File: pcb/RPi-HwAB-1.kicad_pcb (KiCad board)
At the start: 6 copper layers, 65 x 56 mm, 160 parts, among them J1 GPIO, J2 Hirose_FH12-16S, J3 TC2030, U1 CAT24C256, U10 MX25L12835F, U11 INA230AIRGTT, U12 INA230AIRGTT, U13 INA230AIRGTT, U14 MCP9804_DFN, U2 TPSM82903, U3 TLV74312PDBVR, U4 TPSM82903, U5 AP3441SHE-7B, U6 AP3441SHE-7B, U7 XC7A100T-FGG484, U9 MT41K256M16LY, Y1 SiT9365AI-2B2-33E200.000000

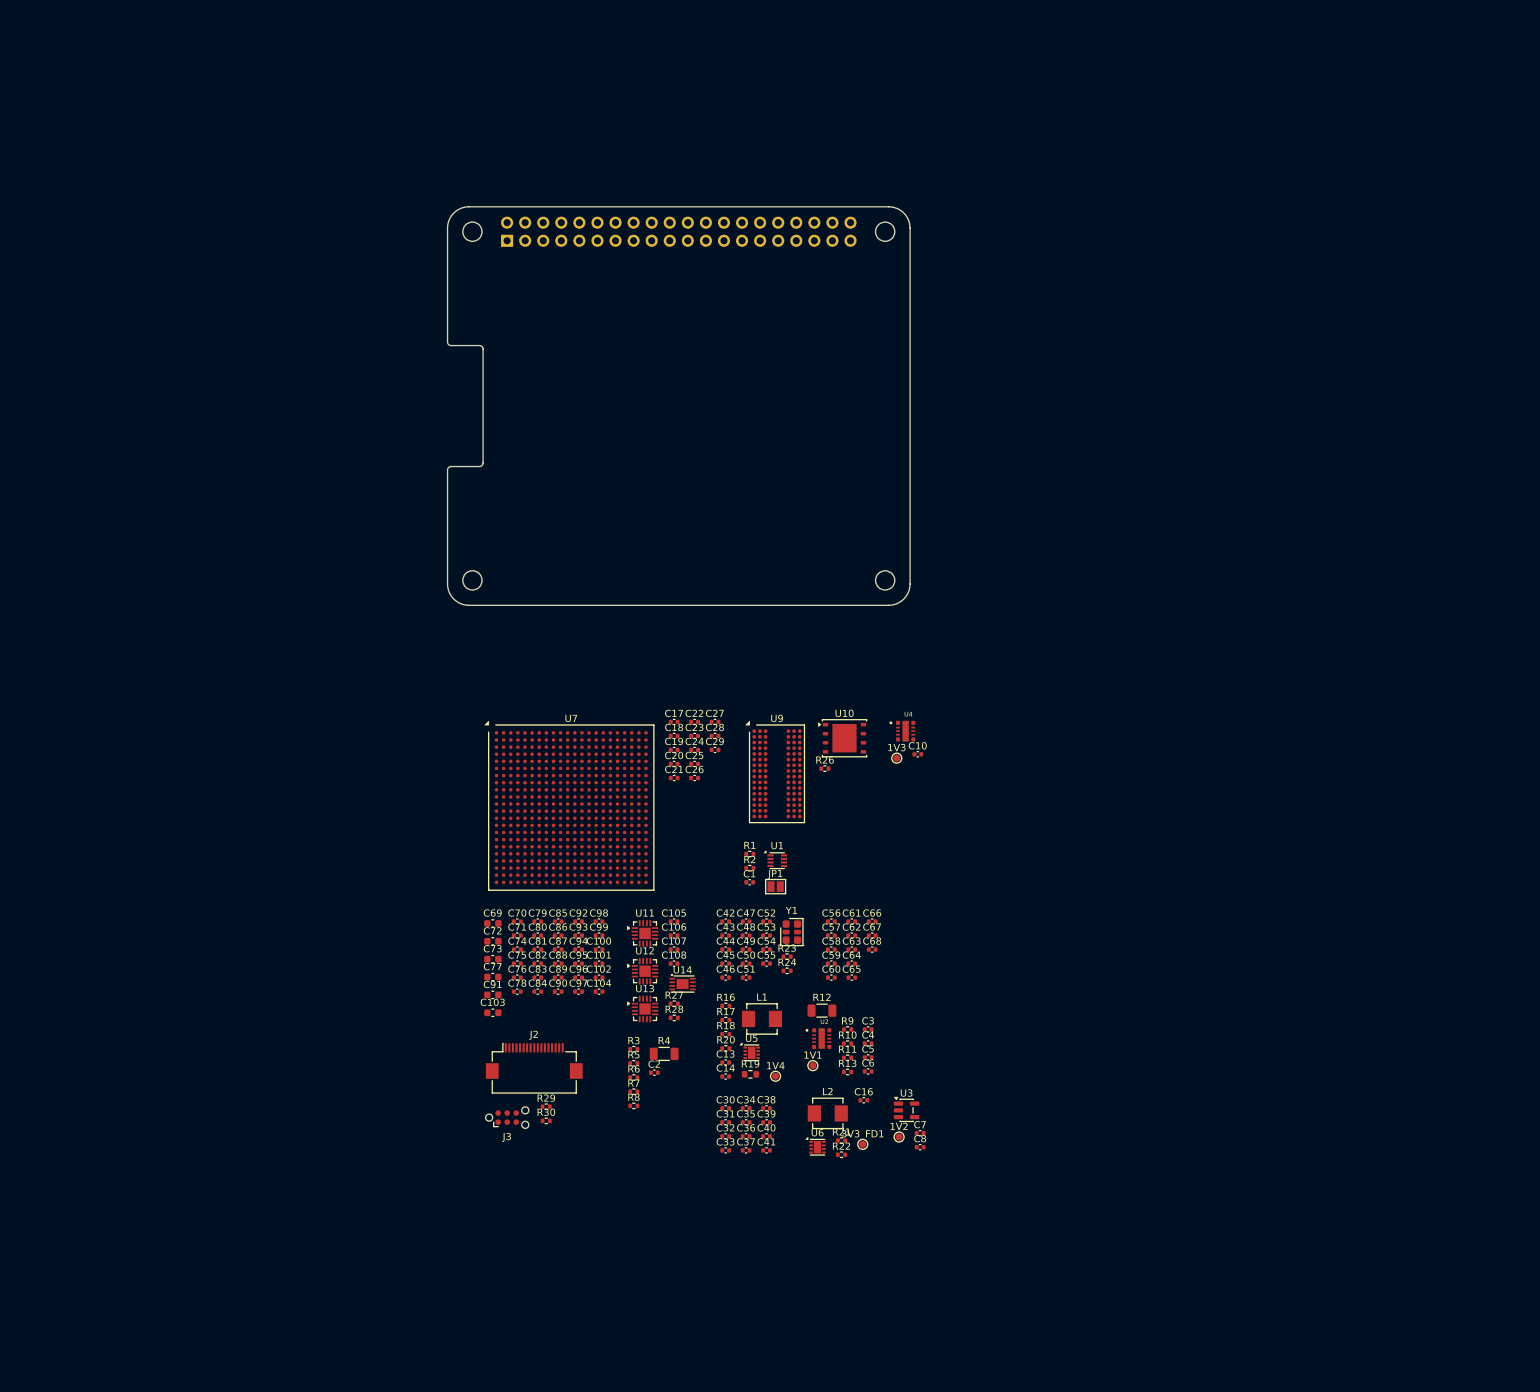
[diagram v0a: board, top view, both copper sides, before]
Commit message: initial layout, dogbone fanout
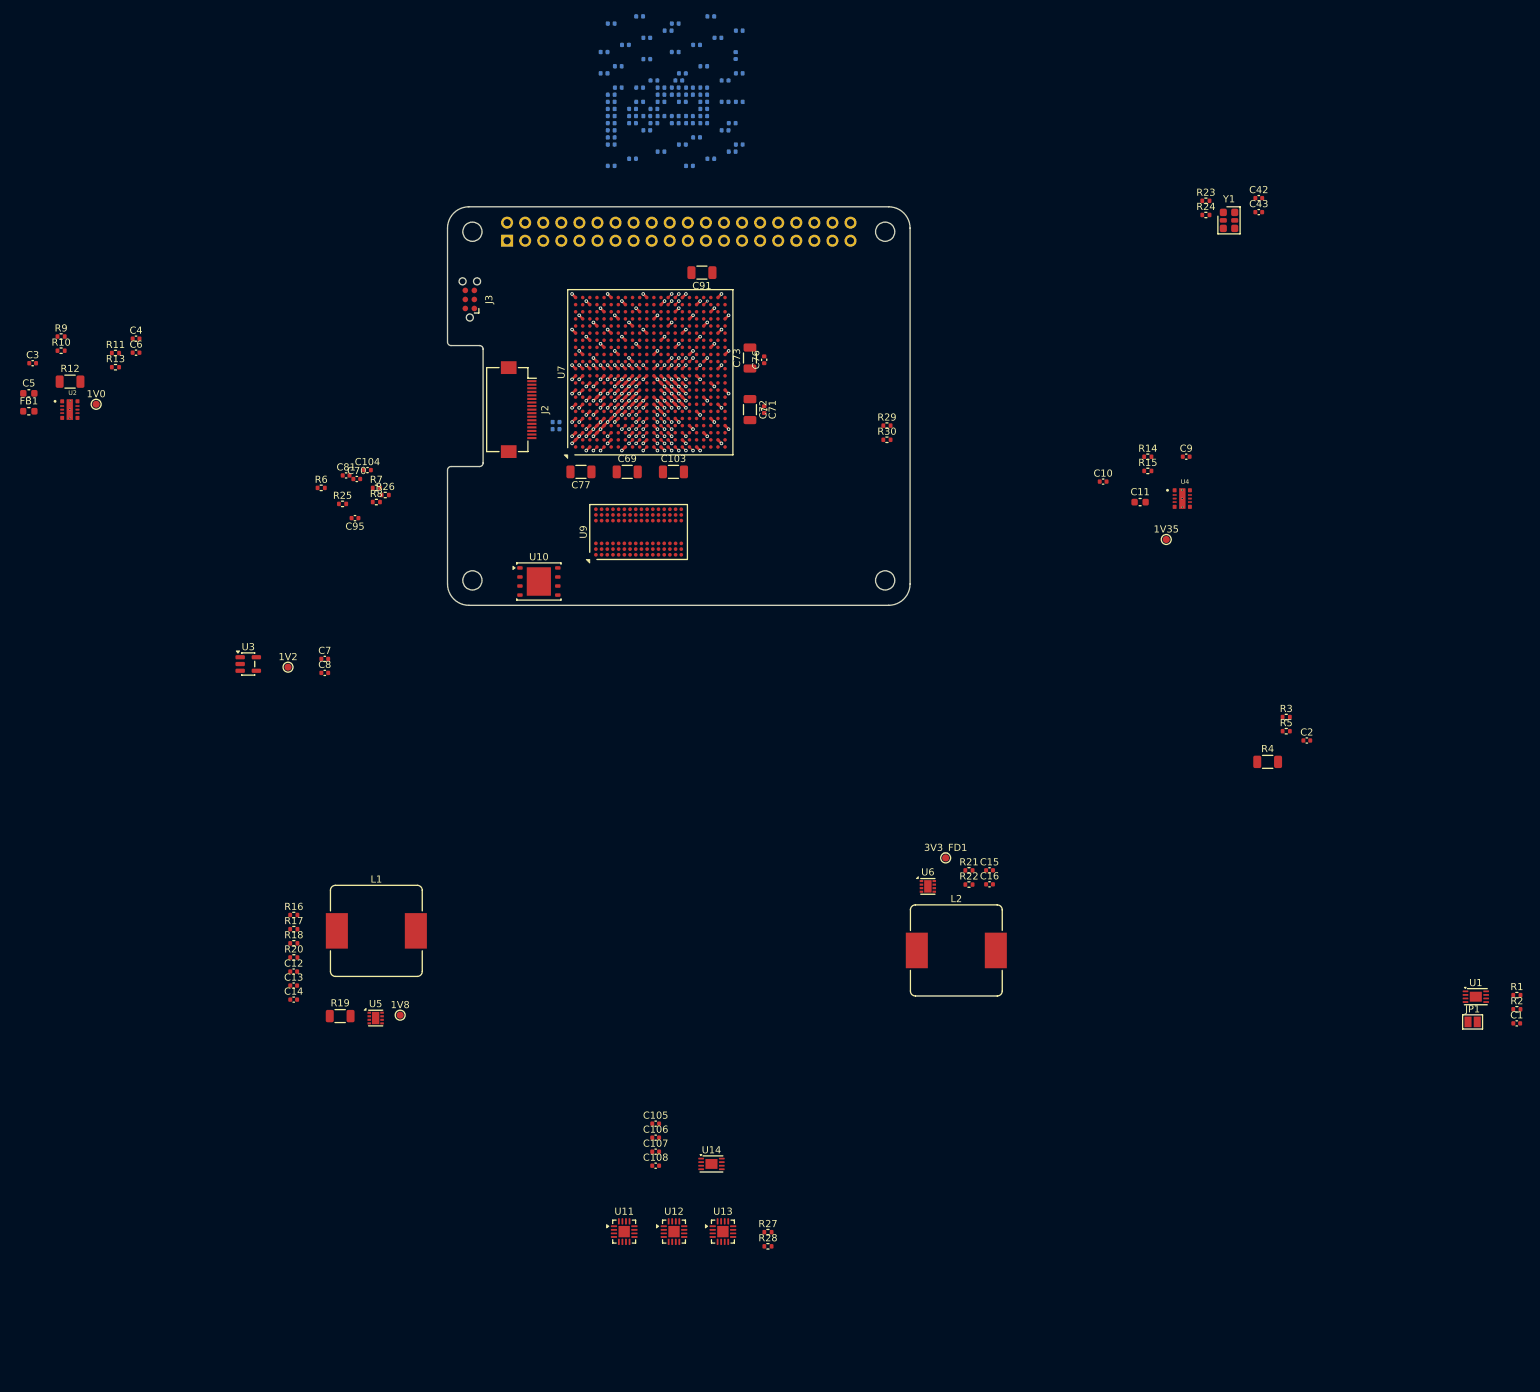
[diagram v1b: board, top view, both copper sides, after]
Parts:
- removed 1V1, 1V3, 1V4: TestPoint, TestPoint:TestPoint_Pad_D1.0mm
- added 1V0: TestPoint, TestPoint:TestPoint_Pad_D1.0mm, F.Cu at (50.6, 71.8)
- added 1V35: TestPoint, TestPoint:TestPoint_Pad_D1.0mm, F.Cu at (201.0, 90.8)
- added 1V8: TestPoint, TestPoint:TestPoint_Pad_D1.0mm, F.Cu at (93.3, 157.6)
- added C11: 22uF, Capacitor_SMD:C_0603_1608Metric, F.Cu at (197.3, 85.5)
- added C12: 10uF, Capacitor_SMD:C_0402_1005Metric, F.Cu at (78.4, 151.5)
- added C15: 10uF, Capacitor_SMD:C_0402_1005Metric, F.Cu at (176.2, 137.2)
- added C9: 10uF, Capacitor_SMD:C_0402_1005Metric, F.Cu at (203.8, 79.1)
- added FB1: 120R @ 100MHz, Inductor_SMD:L_0603_1608Metric, F.Cu at (41.2, 72.7)
- added R14: 15K 1%, Resistor_SMD:R_0402_1005Metric, F.Cu at (198.4, 79.1)
- added R15: 12K 1%, Resistor_SMD:R_0402_1005Metric, F.Cu at (198.4, 81.1)
- added R25: 1K, Resistor_SMD:R_0402_1005Metric, F.Cu at (85.2, 85.8)
- C1: value 100n -> 0.1uF
- C100, C101, C102, C17, C18, C19, C20, C21, C22, C23, C24, C25, C26, C27, C28, C29, C30, C31, C32, C33, C34, C35, C36, C37, C38, C39, C40, C41, C44, C45, C46, C47, C48, C49, C50, C51, C52, C53, C54, C55, C56, C57, C58, C59, C60, C61, C62, C63, C64, C65, C66, C67, C68, C74, C75, C78, C79, C80, C82, C83, C84, C85, C86, C87, C88, C89, C90, C92, C93, C94, C96, C97, C98, C99: moved to B.Cu
- C103, C69, C72, C73, C77, C91: footprint Capacitor_SMD:C_0603_1608Metric -> Capacitor_SMD:C_1206_3216Metric
- C3: footprint library:C_0402_1005Metric -> Capacitor_SMD:C_0402_1005Metric
- C5: footprint library:C_0402_1005Metric -> Capacitor_SMD:C_0603_1608Metric
- L1, L2: footprint Inductor_SMD:L_Vishay_IHLP-1616 -> Inductor_SMD:L_Bourns_SRP1245A
- R10, R29, R6, R7, R8, R9: footprint library:R_0402_1005Metric -> Resistor_SMD:R_0402_1005Metric
- R19: footprint Resistor_SMD:R_0603_1608Metric -> Resistor_SMD:R_1206_3216Metric
- U1: footprint Package_DFN_QFN:DFN-8_2x2mm_P0.5mm -> Package_DFN_QFN:DFN-8-1EP_3x2mm_P0.5mm_EP1.7x1.4mm
- U11, U12, U13: value INA230AIRGTT -> INA230AIRGTR
- U14: value MCP9804_DFN -> MCP9804T-E/MC
- U9: value MT41K256M16LY -> MT41K256M16TW-107:P TR
- moved C37 159.5 mm to (123.0, 18.2)
- moved C41 155.7 mm to (135.0, 21.2), turned to 180 degrees
- moved C32 154.4 mm to (138.0, 20.2), turned to 180 degrees
- moved C36 150.5 mm to (136.0, 24.2), turned to 180 degrees
- moved C5 150.4 mm to (41.2, 70.2)
- moved C3 150.2 mm to (41.7, 66.0)
- moved C39 149.2 mm to (122.0, 25.2), turned to 180 degrees
- moved C30 147.9 mm to (128.0, 23.2), turned to 180 degrees
- moved C40 147.6 mm to (136.0, 27.2), turned to 180 degrees
- moved C33 147.4 mm to (139.0, 29.2)
- moved R9 147.3 mm to (45.7, 62.2)
- moved R10 147.3 mm to (45.7, 64.2)
- moved C35 146.4 mm to (139.0, 26.2), turned to 180 degrees
- moved C34 145.0 mm to (129.0, 26.2), turned to 180 degrees
- moved C38 144.5 mm to (127.0, 27.2), turned to 180 degrees
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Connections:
- C105 pad 1: /Connectors/3V3 -> /Sensors/3V3_RPi
- C106 pad 1: /Connectors/3V3 -> /Sensors/3V3_RPi
- C107 pad 1: /Connectors/3V3 -> /Sensors/3V3_RPi
- C108 pad 1: /Connectors/3V3 -> /Sensors/3V3_RPi
- J1 pad 1: /Connectors/3V3 -> /Connectors/3V3_RPi
- J1 pad 17: /Connectors/3V3 -> /Connectors/3V3_RPi
- R27 pad 1: /Connectors/3V3 -> /Sensors/3V3_RPi
- R28 pad 1: /Connectors/3V3 -> /Sensors/3V3_RPi
- R30 pad 1: /Connectors/3V3 -> /Connectors/3V3_RPi
- U11 pad 8: /Connectors/3V3 -> /Sensors/3V3_RPi
- U12 pad 2: /Connectors/3V3 -> /Sensors/3V3_RPi
- U12 pad 8: /Connectors/3V3 -> /Sensors/3V3_RPi
- U13 pad 2: /Connectors/3V3 -> /Sensors/3V3_RPi
- U13 pad 8: /Connectors/3V3 -> /Sensors/3V3_RPi
- U14 pad 8: /Connectors/3V3 -> /Sensors/3V3_RPi
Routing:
- net GND: track 0.00 -> 79.9 mm, vias 0 -> 90
- net /Main Power/1V0_FD: track 0.00 -> 18.4 mm, vias 0 -> 18
- net /Main Power/3V3_FD: track 0.00 -> 17.7 mm, vias 0 -> 25
- net /Main Power/1V35_DDR: track 0.00 -> 8.49 mm, vias 0 -> 12
- net /Main Power/1V8_FD: track 0.00 -> 4.24 mm, vias 0 -> 6
- net /Main Power/1V2_MGT: track 0.00 -> 4.24 mm, vias 0 -> 6
- net /Main Power/1V0_MGT: track 0.00 -> 3.54 mm, vias 0 -> 5
- net /FPGA/FPGA 3/WEn: track 0.00 -> 0.71 mm, vias 0 -> 1
- net /FPGA/FPGA 3/UDQS_P: track 0.00 -> 0.71 mm, vias 0 -> 1
- net /FPGA/FPGA 3/UDQS_N: track 0.00 -> 0.71 mm, vias 0 -> 1
- net /FPGA/FPGA 3/UDM: track 0.00 -> 0.71 mm, vias 0 -> 1
- net /FPGA/FPGA 3/RESETn: track 0.00 -> 0.71 mm, vias 0 -> 1
- net /FPGA/FPGA 3/RASn: track 0.00 -> 0.71 mm, vias 0 -> 1
- net /FPGA/FPGA 3/ODT: track 0.00 -> 0.71 mm, vias 0 -> 1
- net /FPGA/FPGA 3/LDQS_P: track 0.00 -> 0.71 mm, vias 0 -> 1
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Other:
- copper layers 6 -> 4
- board text removed: "DISPLAY (OPTIONAL)"
- board text removed: "Extend PCB edge 0.5mm if using SMT header"
- board text removed: "PoE"
- board text removed: "RJ45"
- board text removed: "USB"

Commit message: added mig ddr pinout constraints
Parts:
- removed C100, C101, C102, C105, C106, C107, C108, C74, C75, C78, C79, C80, C82, C83, C84, C85, C86, C87, C88, C89, C90, C92, C93, C94, C96, C97, C98, C99: 0.1uF, Capacitor_SMD:C_0402_1005Metric
- removed C103, C72, C73, C77, C91: 47uF, Capacitor_SMD:C_1206_3216Metric
- removed C104, C71, C76, C81, C95: 10uF, Capacitor_SMD:C_0402_1005Metric
- C10, C16: value 4.7nF -> 10uF; footprint Capacitor_SMD:C_0402_1005Metric -> Capacitor_SMD:C_1206_3216Metric
- C11: value 22uF -> 4.7nF; footprint Capacitor_SMD:C_0603_1608Metric -> Capacitor_SMD:C_0402_1005Metric
- C12, C15: value 10uF -> 4.7nF
- C13, C4: value 4.7nF -> 0.1uF
- C14: value 0.1uF -> 10uF; footprint Capacitor_SMD:C_0402_1005Metric -> Capacitor_SMD:C_1206_3216Metric
- C3, C9: value 10uF -> 22uF; footprint Capacitor_SMD:C_0402_1005Metric -> Capacitor_SMD:C_0603_1608Metric
- C37, C38, C67, C68: moved to F.Cu
- C42, C43: moved to B.Cu
- C44, C46, C48, C50, C52, C62: value 0.1uF -> 10uF; footprint Capacitor_SMD:C_0402_1005Metric -> Capacitor_SMD:C_1206_3216Metric; moved to F.Cu
- C45, C47, C49, C51, C57, C63: value 0.1uF -> 4.7uF; footprint Capacitor_SMD:C_0402_1005Metric -> Capacitor_SMD:C_0603_1608Metric; moved to F.Cu
- C5: value 22uF -> 10uF; footprint Capacitor_SMD:C_0603_1608Metric -> Capacitor_SMD:C_1206_3216Metric
- C6: value 0.1uF -> 4.7nF
- C69: value 47uF -> 0.1uF; footprint Capacitor_SMD:C_1206_3216Metric -> Capacitor_SMD:C_0402_1005Metric
- C70: value 10uF -> 0.1uF
- R10: value 15K 1% -> 10K 1%
- R12, R19: value 0.005 -> 10; footprint Resistor_SMD:R_1206_3216Metric -> Resistor_SMD:R_0402_1005Metric
- R13, R20: value 10 -> 15K 1%
- R16: value 30K 1% -> 0.005; footprint Resistor_SMD:R_0402_1005Metric -> Resistor_SMD:R_1206_3216Metric
- R17: value 15K 1% -> 30K 1%
- R29: value 100K -> 2.2K
- R3: value 10 -> 0.003 1%; footprint Resistor_SMD:R_0402_1005Metric -> Resistor_SMD:R_1206_3216Metric
- R30: value 2.2K -> 100K
- R4: value 0.003 1% -> 10; footprint Resistor_SMD:R_1206_3216Metric -> Resistor_SMD:R_0402_1005Metric
- R9: value 10K 1% -> 0.005; footprint Resistor_SMD:R_0402_1005Metric -> Resistor_SMD:R_1206_3216Metric
- U10: value MX25L12835F -> MT41K256M16TW-107:P TR; footprint Package_SON:WSON-8-1EP_6x5mm_P1.27mm_EP3.4x4mm -> Package_BGA:Micron_FBGA-96_7.5x13.5mm_Layout9x16_P0.8mm
- U12: value INA230AIRGTR -> MCP9804T-E/MC; footprint Package_DFN_QFN:VQFN-16-1EP_3x3mm_P0.5mm_EP1.6x1.6mm -> Package_DFN_QFN:DFN-8-1EP_3x2mm_P0.5mm_EP1.7x1.4mm
- U14: value MCP9804T-E/MC -> INA230AIRGTR; footprint Package_DFN_QFN:DFN-8-1EP_3x2mm_P0.5mm_EP1.7x1.4mm -> Package_DFN_QFN:VQFN-16-1EP_3x3mm_P0.5mm_EP1.6x1.6mm
- U9: value MT41K256M16TW-107:P TR -> MX25L12835F; footprint Package_BGA:Micron_FBGA-96_7.5x13.5mm_Layout9x16_P0.8mm -> Package_SON:WSON-8-1EP_6x5mm_P1.27mm_EP3.4x4mm
- moved C55 176.0 mm to (92.8, 208.2)
- moved C56 176.0 mm to (85.8, 201.2)
- moved C58 168.6 mm to (93.2, 199.2)
- moved C59 168.6 mm to (93.2, 198.2)
- moved C60 168.6 mm to (96.2, 197.2)
- moved C61 168.6 mm to (93.2, 197.2)
- moved C64 168.6 mm to (96.2, 198.2)
- moved C65 168.6 mm to (93.2, 194.2)
- moved C66 168.6 mm to (93.2, 196.2)
- moved C53 161.0 mm to (89.8, 188.8)
- moved C54 161.0 mm to (94.8, 186.8)
- moved C42 88.7 mm to (131.5, 75.2)
- moved C43 86.7 mm to (131.5, 71.2)
- moved C30 72.9 mm to (159.5, 89.0)
- moved C29 67.7 mm to (159.5, 87.5)
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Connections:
- net +3V3 renamed 3V3_RPi
- C10 pad 1: Net-(U4-SS/TR) -> /Main Power/5V0_N
- C11 pad 1: /Main Power/1V35_DDR -> Net-(U4-SS/TR)
- C12 pad 1: /Main Power/5V0_N -> /Main Power/1V8/1V8_P
- C12 pad 2: GND -> /Main Power/1V8/1V8_FB
- C13 pad 1: /Main Power/1V8/1V8_P -> /Main Power/1V8_SENS_N
- C13 pad 2: /Main Power/1V8/1V8_FB -> /Main Power/1V8_SENS_P
- C14 pad 1: /Main Power/1V8_SENS_N -> /Main Power/5V0_N
- C14 pad 2: /Main Power/1V8_SENS_P -> GND
- C15 pad 1: /Main Power/5V0_N -> /Main Power/3V3_FD
- C15 pad 2: GND -> /Main Power/3V3/3V3_FB
- C16 pad 1: /Main Power/3V3_FD -> /Main Power/5V0_N
- C16 pad 2: /Main Power/3V3/3V3_FB -> GND
- C29 pad 1: GND -> Net-(U7E-IO_L12N_T1_MRCC_34)
- C29 pad 2: /Main Power/3V3_FD -> Net-(Y1-OUT-)
- C3 pad 1: /Main Power/5V0_N -> /Main Power/1V0/1V0_P
- C30 pad 1: GND -> Net-(U7E-IO_L12P_T1_MRCC_34)
- C30 pad 2: /Main Power/3V3_FD -> Net-(Y1-OUT+)
- C31 pad 2: /Main Power/3V3_FD -> /Main Power/1V35_DDR
- C32 pad 2: /Main Power/3V3_FD -> /Main Power/1V35_DDR
- C33 pad 2: /Main Power/3V3_FD -> /Main Power/1V35_DDR
- C34 pad 2: /Main Power/3V3_FD -> /Main Power/1V35_DDR
- C35 pad 2: /Main Power/3V3_FD -> /Main Power/1V35_DDR
- C36 pad 2: /Main Power/3V3_FD -> /Main Power/1V35_DDR
- C37 pad 1: GND -> /FPGA/FPGA 4/F2P_P
- C37 pad 2: /Main Power/3V3_FD -> /Connectors/PCIE.F2P_N
- C38 pad 1: GND -> /FPGA/FPGA 4/F2P_N
- C38 pad 2: /Main Power/3V3_FD -> /Connectors/PCIE.F2P_P
- C39 pad 2: /Main Power/3V3_FD -> /Main Power/1V0_MGT
- C4 pad 1: Net-(U2-SS/TR) -> /Main Power/1V0_SENS_N
- C4 pad 2: GND -> /Main Power/1V0_SENS_P
- C40 pad 2: /Main Power/3V3_FD -> /Main Power/1V0_MGT
- C41 pad 2: /Main Power/3V3_FD -> /Main Power/1V2_MGT
- C42 pad 1: Net-(U7E-IO_L12N_T1_MRCC_34) -> GND
- C42 pad 2: Net-(Y1-OUT-) -> /Main Power/1V2_MGT
- C43 pad 1: Net-(U7E-IO_L12P_T1_MRCC_34) -> GND
- C43 pad 2: Net-(Y1-OUT+) -> /Main Power/1V2_MGT
- C44 pad 1: GND -> /Main Power/1V0_MGT
- C44 pad 2: /Main Power/1V35_DDR -> GND
- C45 pad 1: GND -> /Main Power/1V0_MGT
- C45 pad 2: /Main Power/1V35_DDR -> GND
- C46 pad 1: GND -> /Main Power/1V2_MGT
- C46 pad 2: /Main Power/1V35_DDR -> GND
- C47 pad 1: GND -> /Main Power/1V2_MGT
- C47 pad 2: /Main Power/1V35_DDR -> GND
- C48 pad 1: GND -> /Main Power/3V3_FD
- C48 pad 2: /Main Power/1V35_DDR -> GND
- C49 pad 1: GND -> /Main Power/3V3_FD
- C49 pad 2: /Main Power/1V35_DDR -> GND
- C5 pad 1: /Main Power/1V0/1V0_P -> /Main Power/5V0_N
- C50 pad 1: GND -> /Main Power/1V35_DDR
- C50 pad 2: /Main Power/1V35_DDR -> GND
- C51 pad 1: GND -> /Main Power/1V35_DDR
- C51 pad 2: /Main Power/1V35_DDR -> GND
- C52 pad 1: GND -> /Main Power/1V0_FD
- C52 pad 2: /Main Power/1V35_DDR -> GND
- C53 pad 2: /Main Power/1V35_DDR -> /Main Power/1V0_FD
- C54 pad 2: /Main Power/1V35_DDR -> /Main Power/1V0_FD
- C55 pad 2: /Main Power/1V35_DDR -> /Main Power/1V0_FD
- C56 pad 2: /Main Power/1V0_MGT -> /Main Power/1V0_FD
- C57 pad 1: GND -> /Main Power/1V0_FD
- C57 pad 2: /Main Power/1V2_MGT -> GND
- C58 pad 2: /Main Power/1V0_MGT -> /Main Power/1V0_FD
- C59 pad 2: /Main Power/1V2_MGT -> /Main Power/1V0_FD
- C6 pad 1: /Main Power/1V0_SENS_N -> Net-(U2-SS/TR)
- C6 pad 2: /Main Power/1V0_SENS_P -> GND
- C60 pad 2: /Main Power/1V0_MGT -> /Main Power/1V0_FD
- C61 pad 2: /Main Power/1V2_MGT -> /Main Power/1V0_FD
- C62 pad 1: GND -> /Main Power/1V8_FD
- C62 pad 2: /Main Power/1V0_MGT -> GND
- C63 pad 1: GND -> /Main Power/1V8_FD
- C63 pad 2: /Main Power/1V2_MGT -> GND
- C64 pad 2: /Main Power/1V0_MGT -> /Main Power/1V8_FD
- C65 pad 2: /Main Power/1V2_MGT -> /Main Power/1V8_FD
- C66 pad 2: /Main Power/1V2_MGT -> /Main Power/1V8_FD
- C67 pad 1: /FPGA/FPGA 4/F2P_N -> /Connectors/3V3_RPi
- C67 pad 2: /Connectors/PCIE.F2P_P -> GND
- C68 pad 1: /FPGA/FPGA 4/F2P_P -> /Connectors/3V3_RPi
- C68 pad 2: /Connectors/PCIE.F2P_N -> GND
- C69 pad 1: /Main Power/1V0_MGT -> /Connectors/3V3_RPi
- C70 pad 1: /Main Power/1V0_MGT -> /Connectors/3V3_RPi
- C9 pad 1: /Main Power/5V0_N -> /Main Power/1V35_DDR
- J3 pad 1: /Connectors/3V3 -> /Connectors/3V3_RPi
- R10 pad 1: /Main Power/1V0/1V0_FB -> /Main Power/1V0/1V0_P
- R10 pad 2: GND -> /Main Power/1V0/1V0_FB
- R12 pad 1: /Main Power/1V0_FD -> /Main Power/1V0_SENS_P
- R12 pad 2: /Main Power/1V0/1V0_P -> /Main Power/1V0_FD
- R13 pad 1: /Main Power/1V0_SENS_P -> /Main Power/1V0/1V0_FB
- R13 pad 2: /Main Power/1V0_FD -> GND
- R16 pad 1: /Main Power/1V8/1V8_P -> /Main Power/1V8_FD
- R16 pad 2: /Main Power/1V8/1V8_FB -> /Main Power/1V8/1V8_P
- R17 pad 1: /Main Power/1V8/1V8_FB -> /Main Power/1V8/1V8_P
- R17 pad 2: GND -> /Main Power/1V8/1V8_FB
- R19 pad 1: /Main Power/1V8_FD -> /Main Power/1V8_SENS_N
- R19 pad 2: /Main Power/1V8/1V8_P -> /Main Power/1V8_FD
- R20 pad 1: /Main Power/1V8_SENS_N -> /Main Power/1V8/1V8_FB
- R20 pad 2: /Main Power/1V8_FD -> GND
- R26 pad 1: Net-(U9-ZQ) -> Net-(U10-ZQ)
- R27 pad 1: /Sensors/3V3_RPi -> /Connectors/3V3_RPi
- R28 pad 1: /Sensors/3V3_RPi -> /Connectors/3V3_RPi
- R29 pad 1: GND -> /Main Power/3V3_FD
- R29 pad 2: /Connectors/PCIE.PWR_EN -> /Connectors/PCIE.DET_WAKE
- R3 pad 1: /Main Power/5V0_SENS_N -> /Connectors/5V0
- R3 pad 2: /Connectors/5V0 -> /Main Power/5V0_N
- R30 pad 1: /Connectors/3V3_RPi -> GND
- R30 pad 2: /Connectors/PCIE.DET_WAKE -> /Connectors/PCIE.PWR_EN
- R4 pad 1: /Connectors/5V0 -> /Main Power/5V0_SENS_N
- R4 pad 2: /Main Power/5V0_N -> /Connectors/5V0
- R9 pad 1: /Main Power/1V0/1V0_P -> /Main Power/1V0_FD
- R9 pad 2: /Main Power/1V0/1V0_FB -> /Main Power/1V0/1V0_P
- U11 pad 8: /Sensors/3V3_RPi -> /Connectors/3V3_RPi
- U12 pad 1: GND -> /Connectors/I2C1.SDA
- U12 pad 2: /Sensors/3V3_RPi -> /Connectors/I2C1.SCL
- U12 pad 4: /Connectors/I2C1.SDA -> GND
- U12 pad 5: /Connectors/I2C1.SCL -> GND
- U12 pad 8: /Sensors/3V3_RPi -> /Connectors/3V3_RPi
- U12 pad 9: (no net) -> GND
- U13 pad 11: /Main Power/1V8_SENS_P -> /Main Power/1V0_SENS_P
- U13 pad 12: /Main Power/1V8_SENS_N -> /Main Power/1V0_SENS_N
- U13 pad 13: /Main Power/1V8_SENS_P -> /Main Power/1V0_SENS_P
- U13 pad 2: /Sensors/3V3_RPi -> /Connectors/3V3_RPi
- U13 pad 8: /Sensors/3V3_RPi -> /Connectors/3V3_RPi
- U14 pad 1: /Connectors/I2C1.SDA -> /Connectors/3V3_RPi
- U14 pad 2: /Connectors/I2C1.SCL -> GND
- U14 pad 4: GND -> /Connectors/I2C1.SDA
- U14 pad 5: GND -> /Connectors/I2C1.SCL
- U14 pad 8: /Sensors/3V3_RPi -> /Connectors/3V3_RPi
- U14 pad 9: GND -> (no net)
- U7 pad AA1: unconnected-(U7E-IO_L7P_T1_34-PadAA1) -> /FPGA/FPGA 3/A13
- U7 pad AA8: unconnected-(U7E-IO_L22P_T3_34-PadAA8) -> /FPGA/FPGA 3/DDR_RASn
- U7 pad AB1: unconnected-(U7E-IO_L7N_T1_34-PadAB1) -> /FPGA/FPGA 3/A14
- U7 pad AB6: unconnected-(U7E-IO_L20N_T3_34-PadAB6) -> /FPGA/FPGA 3/DDR_BA1
- U7 pad AB7: unconnected-(U7E-IO_L20P_T3_34-PadAB7) -> /FPGA/FPGA 3/DDR_BA0
- U7 pad AB8: unconnected-(U7E-IO_L22N_T3_34-PadAB8) -> /FPGA/FPGA 3/DDR_CASn
- U7 pad D1: /FPGA/FPGA 3/LDQS_N -> /FPGA/FPGA 3/DDR_LDQS_N
- U7 pad E1: /FPGA/FPGA 3/LDQS_P -> /FPGA/FPGA 3/DDR_LDQS_P
- U7 pad F3: /FPGA/FPGA 3/LDM -> /FPGA/FPGA 3/DDR_LDM
- U7 pad H4: /FPGA/FPGA 3/UDM -> /FPGA/FPGA 3/DDR_UDM
- U7 pad J2: /FPGA/FPGA 3/UDQS_N -> /FPGA/FPGA 3/DDR_UDQS_N
- U7 pad J4: /FPGA/FPGA 3/A1 -> unconnected-(U7F-IO_L13N_T2_MRCC_35-PadJ4)
- U7 pad J6: /FPGA/FPGA 3/A9 -> unconnected-(U7F-IO_L17N_T2_35-PadJ6)
- U7 pad K2: /FPGA/FPGA 3/UDQS_P -> /FPGA/FPGA 3/DDR_UDQS_P
- U7 pad K3: /FPGA/FPGA 3/A3 -> unconnected-(U7F-IO_L14N_T2_SRCC_35-PadK3)
- U7 pad K4: /FPGA/FPGA 3/A0 -> unconnected-(U7F-IO_L13P_T2_MRCC_35-PadK4)
- U7 pad K6: /FPGA/FPGA 3/A8 -> unconnected-(U7F-IO_L17P_T2_35-PadK6)
- U7 pad L1: /FPGA/FPGA 3/A5 -> unconnected-(U7F-IO_L15N_T2_DQS_35-PadL1)
- U7 pad L3: /FPGA/FPGA 3/A2 -> unconnected-(U7F-IO_L14P_T2_SRCC_35-PadL3)
- U7 pad L4: /FPGA/FPGA 3/A11 -> unconnected-(U7F-IO_L18N_T2_35-PadL4)
- U7 pad L5: /FPGA/FPGA 3/A10 -> unconnected-(U7F-IO_L18P_T2_35-PadL5)
- U7 pad M1: /FPGA/FPGA 3/A4 -> unconnected-(U7F-IO_L15P_T2_DQS_35-PadM1)
- U7 pad M2: /FPGA/FPGA 3/A7 -> unconnected-(U7F-IO_L16N_T2_35-PadM2)
- U7 pad M3: /FPGA/FPGA 3/A6 -> unconnected-(U7F-IO_L16P_T2_35-PadM3)
- U7 pad M5: /FPGA/FPGA 3/CKE -> unconnected-(U7F-IO_L23N_T3_35-PadM5)
- U7 pad M6: /FPGA/FPGA 3/ODT -> unconnected-(U7F-IO_L23P_T3_35-PadM6)
- U7 pad N2: /FPGA/FPGA 3/WEn -> unconnected-(U7F-IO_L22N_T3_35-PadN2)
- U7 pad N3: /FPGA/FPGA 3/BA0 -> unconnected-(U7F-IO_L19N_T3_VREF_35-PadN3)
- U7 pad N4: /FPGA/FPGA 3/A12 -> unconnected-(U7F-IO_L19P_T3_35-PadN4)
- U7 pad N5: /FPGA/FPGA 3/CKn -> unconnected-(U7F-IO_L24N_T3_35-PadN5)
- U7 pad P1: /FPGA/FPGA 3/BA2 -> unconnected-(U7F-IO_L20N_T3_35-PadP1)
- U7 pad P2: /FPGA/FPGA 3/CASn -> unconnected-(U7F-IO_L22P_T3_35-PadP2)
- U7 pad P4: /FPGA/FPGA 3/RASn -> unconnected-(U7F-IO_L21N_T3_DQS_35-PadP4)
- U7 pad P5: /FPGA/FPGA 3/CSn -> unconnected-(U7F-IO_L21P_T3_DQS_35-PadP5)
- U7 pad P6: /FPGA/FPGA 3/CKp -> unconnected-(U7F-IO_L24P_T3_35-PadP6)
- U7 pad R1: /FPGA/FPGA 3/BA1 -> unconnected-(U7F-IO_L20P_T3_35-PadR1)
- U7 pad R2: unconnected-(U7E-IO_L3N_T0_DQS_34-PadR2) -> /FPGA/FPGA 3/A6
- U7 pad R3: unconnected-(U7E-IO_L3P_T0_DQS_34-PadR3) -> /FPGA/FPGA 3/A5
- U7 pad T1: /FPGA/FPGA 3/A13 -> /FPGA/FPGA 3/A1
- U7 pad T3: /FPGA/FPGA 3/RESETn -> /FPGA/FPGA 3/A0
- U7 pad U1: /FPGA/FPGA 3/A14 -> /FPGA/FPGA 3/A2
- U7 pad U2: unconnected-(U7E-IO_L2P_T0_34-PadU2) -> /FPGA/FPGA 3/A3
- U7 pad U3: unconnected-(U7E-IO_L6P_T0_34-PadU3) -> /FPGA/FPGA 3/A11
- U7 pad U7: unconnected-(U7E-IO_25_34-PadU7) -> /FPGA/FPGA 3/DDR_CKn
- U7 pad V2: unconnected-(U7E-IO_L2N_T0_34-PadV2) -> /FPGA/FPGA 3/A4
- U7 pad V3: unconnected-(U7E-IO_L6N_T0_VREF_34-PadV3) -> /FPGA/FPGA 3/A12
- U7 pad V8: unconnected-(U7E-IO_L21N_T3_DQS_34-PadV8) -> /FPGA/FPGA 3/DDR_CSn
- U7 pad V9: unconnected-(U7E-IO_L21P_T3_DQS_34-PadV9) -> /FPGA/FPGA 3/DDR_BA2
- U7 pad W1: unconnected-(U7E-IO_L5P_T0_34-PadW1) -> /FPGA/FPGA 3/A9
- U7 pad W2: unconnected-(U7E-IO_L4P_T0_34-PadW2) -> /FPGA/FPGA 3/A7
- U7 pad W7: unconnected-(U7E-IO_L19N_T3_VREF_34-PadW7) -> /FPGA/FPGA 3/DDR_RESETn
- U7 pad W9: unconnected-(U7E-IO_L24P_T3_34-PadW9) -> /FPGA/FPGA 3/DDR_CKE
- U7 pad Y1: unconnected-(U7E-IO_L5N_T0_34-PadY1) -> /FPGA/FPGA 3/A10
- U7 pad Y2: unconnected-(U7E-IO_L4N_T0_34-PadY2) -> /FPGA/FPGA 3/A8
- U7 pad Y7: unconnected-(U7E-IO_L23N_T3_34-PadY7) -> /FPGA/FPGA 3/DDR_ODT
- U7 pad Y8: unconnected-(U7E-IO_L23P_T3_34-PadY8) -> /FPGA/FPGA 3/DDR_WEn
- U7 pad Y9: unconnected-(U7E-IO_L24N_T3_34-PadY9) -> /FPGA/FPGA 3/DDR_CKp
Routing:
- net /Connectors/PCIE.CLK_N: track 0.00 -> 27.5 mm, vias 0 -> 2
- net /Connectors/PCIE.CLK_P: track 0.00 -> 26.5 mm, vias 0 -> 2
- net /Connectors/PCIE.P2F_N: track 0.00 -> 20.9 mm
- net /Connectors/PCIE.P2F_P: track 0.00 -> 19.7 mm
- net /Connectors/PCIE.F2P_P: track 0.00 -> 17.1 mm, vias 0 -> 2
- net /Connectors/PCIE.F2P_N: track 0.00 -> 17.1 mm, vias 0 -> 2
- net GND: track 79.9 -> 96.8 mm
- net /Main Power/3V3_FD: track 17.7 -> 30.8 mm
- net /FPGA/FPGA 3/DQ13: track 0.00 -> 7.41 mm, vias 0 -> 2
- net /FPGA/FPGA 3/DQ12: track 0.00 -> 6.37 mm, vias 0 -> 2
- net /FPGA/FPGA 4/F2P_P: track 0.00 -> 5.66 mm
- net /FPGA/FPGA 4/F2P_N: track 0.00 -> 5.62 mm
- net /Main Power/1V35_DDR: track 8.49 -> 12.8 mm
- net /FPGA/FPGA 3/DQ15: track 0.00 -> 3.97 mm, vias 0 -> 2
- net /FPGA/FPGA 3/DQ14: track 0.00 -> 3.97 mm, vias 0 -> 2
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- added copper zone on In3.Cu, net /Main Power/1V0_FD
- added copper zone on In3.Cu, net /Main Power/1V0_MGT
- added copper zone on In3.Cu, net /Main Power/1V2_MGT
- added copper zone on In3.Cu, net /Main Power/1V35_DDR
- added copper zone on In3.Cu, net /Main Power/1V8_FD
- added copper zone on In3.Cu, net /Main Power/3V3_FD
- added copper zone on B.Cu, net GND
- added copper zone on F.Cu, net GND
- added copper zone on In1.Cu, net GND
- added copper zone on In2.Cu, net GND
- added copper zone on In3.Cu, net GND
- added copper zone on In4.Cu, net GND
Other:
- copper layers 4 -> 6
